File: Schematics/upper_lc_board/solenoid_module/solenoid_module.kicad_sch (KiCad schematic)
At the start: 21 parts

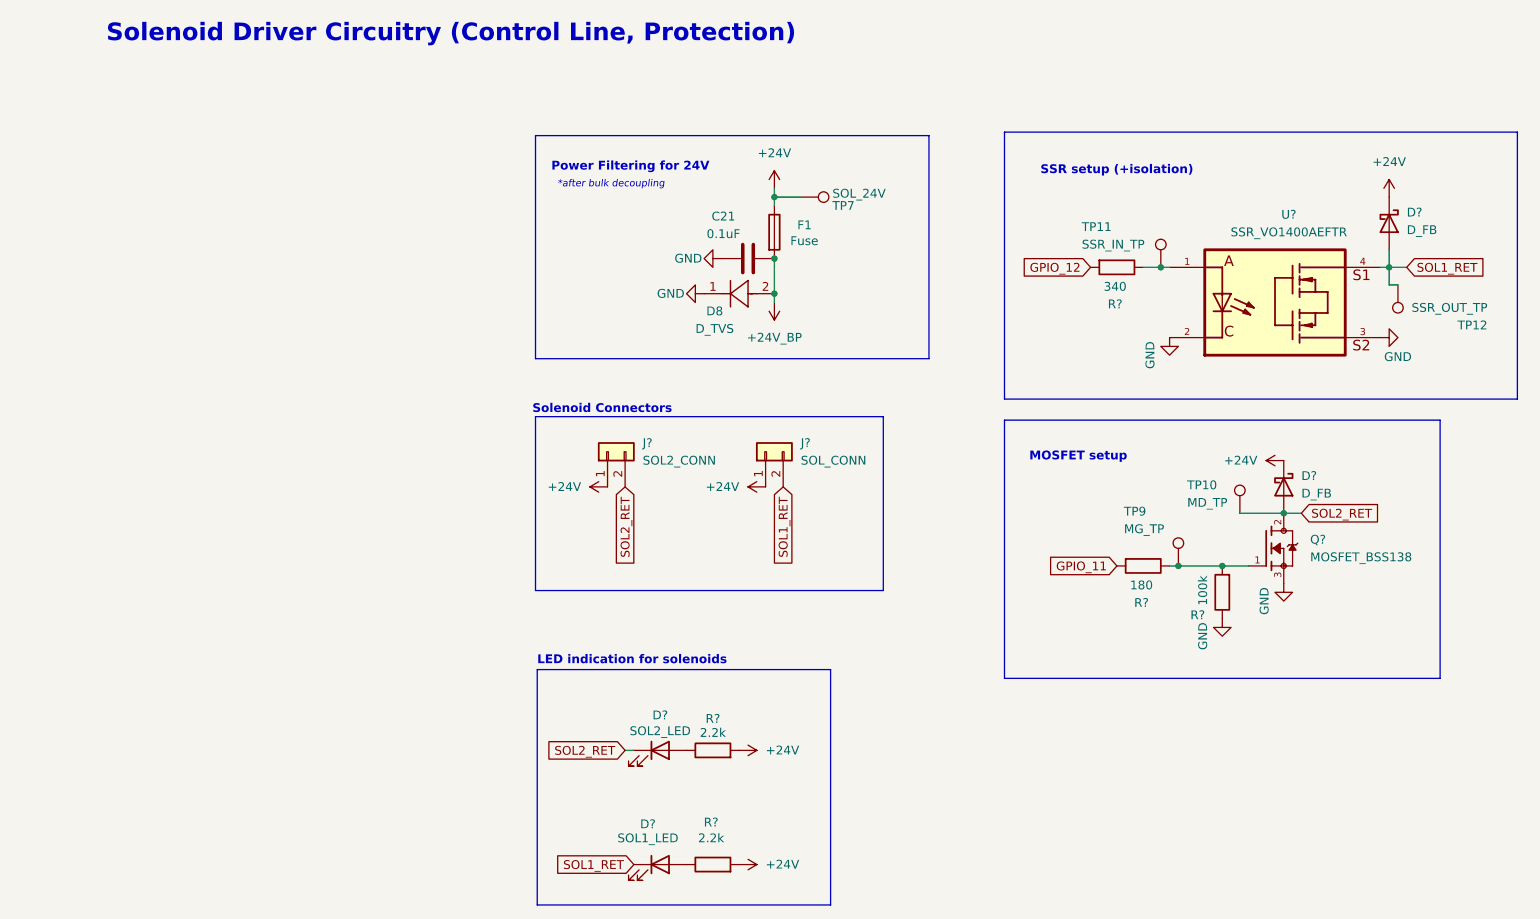
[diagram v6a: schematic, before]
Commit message: Updated all gpio for better routing, > - removed diode array, and 5v sensing > - added dedicated clk generator for adc
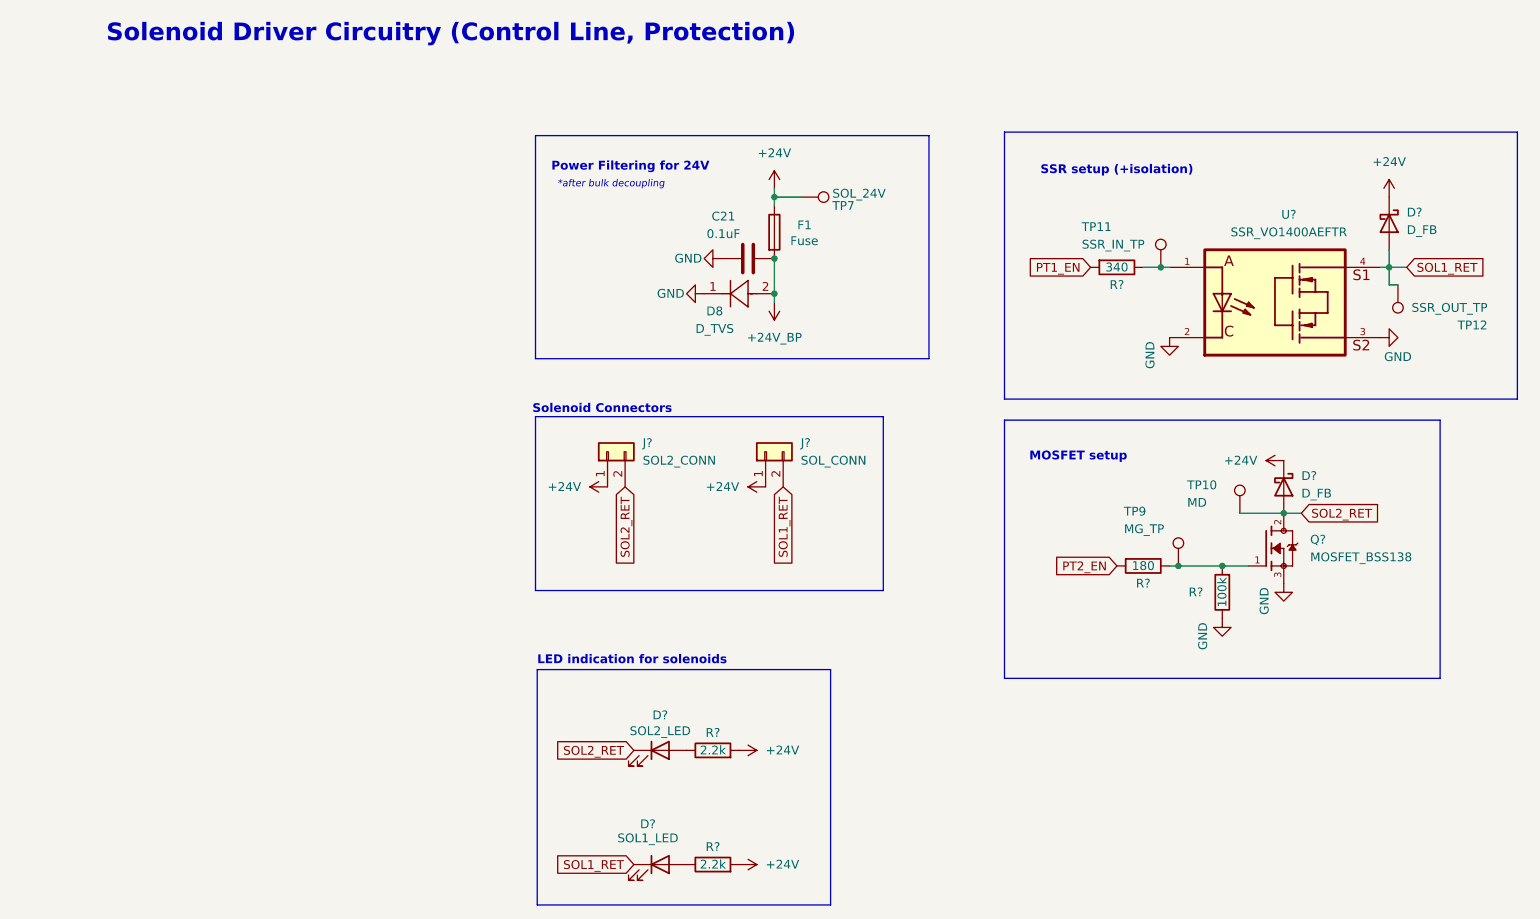
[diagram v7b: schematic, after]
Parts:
- TP10: value MD_TP -> MD
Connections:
- net GPIO_11 renamed PT2_EN
- net GPIO_12 renamed PT1_EN
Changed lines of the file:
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@@
-	(wire
-		(pts
-			(xy 90.17 125.73) (xy 91.44 125.73)
-		)
-		(stroke
-			(width 0)
-			(type default)
-		)
-	)
 	(wire
 		(pts
@@
 		)
 	)
-	(global_label "GPIO_11"
+	(global_label "PT1_EN"
 		(shape input)
-		(at 161.29 99.06 180)
+		(at 157.48 55.88 180)
 		(fields_autoplaced yes)
 		(effects
@@
 		)
 		(property "Intersheetrefs" "${INTERSHEET_REFS}"
-			(at 150.4429 99.06 0)
+			(at 147.6006 55.88 0)
 			(effects
 				(font
@@
 		)
 	)
+	(global_label "PT2_EN"
+		(shape input)
+		(at 161.29 99.06 180)
+		(fields_autoplaced yes)
+		(effects
+			(font
+				(size 1.27 1.27)
+			)
+			(justify right)
+		)
+		(property "Intersheetrefs" "${INTERSHEET_REFS}"
+			(at 151.4106 99.06 0)
+			(effects
+				(font
+					(size 1.27 1.27)
+				)
+				(justify right)
+				(hide yes)
+			)
+		)
+	)
 	(global_label "SOL1_RET"
 		(shape input)
@@
 		)
 	)
-	(global_label "GPIO_12"
-		(shape input)
-		(at 157.48 55.88 180)
-		(fields_autoplaced yes)
-		(effects
-			(font
-				(size 1.27 1.27)
-			)
-			(justify right)
-		)
-		(property "Intersheetrefs" "${INTERSHEET_REFS}"
-			(at 146.6329 55.88 0)
-			(effects
-				(font
-					(size 1.27 1.27)
-				)
-				(justify right)
-				(hide yes)
-			)
-		)
-	)
 	(global_label "SOL2_RET"
 		(shape input)
@@
 	(global_label "SOL2_RET"
 		(shape input)
-		(at 90.17 125.73 180)
+		(at 91.44 125.73 180)
 		(fields_autoplaced yes)
 		(effects
@@
 		)
 		(property "Intersheetrefs" "${INTERSHEET_REFS}"
-			(at 78.053 125.73 0)
+			(at 79.323 125.73 0)
 			(effects
 				(font
@@
 		(dnp no)
 		(property "Reference" "R?"
-			(at 161.036 61.214 90)
+			(at 161.29 58.42 90)
 			(effects
 				(font
@@
 		)
 		(property "Value" "340"
-			(at 161.036 58.674 90)
+			(at 161.29 55.88 90)
 			(effects
 				(font
@@
 			)
 		)
-		(property "Value" "MD_TP"
+		(property "Value" "MD"
 			(at 171.45 89.916 0)
 			(effects
@@
 		(dnp no)
 		(property "Reference" "R?"
-			(at 102.616 136.144 90)
+			(at 102.87 139.7 90)
 			(effects
 				(font
@@
 		)
 		(property "Value" "2.2k"
-			(at 102.616 138.43 90)
+			(at 102.87 142.24 90)
 			(effects
 				(font
@@
 		(dnp no)
 		(property "Reference" "R?"
-			(at 172.974 106.172 0)
+			(at 172.72 102.87 0)
 			(effects
 				(font
@@
 		)
 		(property "Value" "100k"
-			(at 173.736 102.616 90)
+			(at 176.53 102.87 90)
 			(effects
 				(font
@@
 		(dnp no)
 		(property "Reference" "R?"
-			(at 164.846 104.394 90)
+			(at 165.1 101.6 90)
 			(effects
 				(font
@@
 		)
 		(property "Value" "180"
-			(at 164.846 101.854 90)
+			(at 165.1 99.06 90)
 			(effects
 				(font
@@
 		(dnp no)
 		(property "Reference" "R?"
-			(at 102.87 121.158 90)
+			(at 102.87 123.19 90)
 			(effects
 				(font
@@
 		)
 		(property "Value" "2.2k"
-			(at 102.87 123.19 90)
-			(effects
-				(font
+			(at 102.87 125.73 90)
+			(effects
+				(font

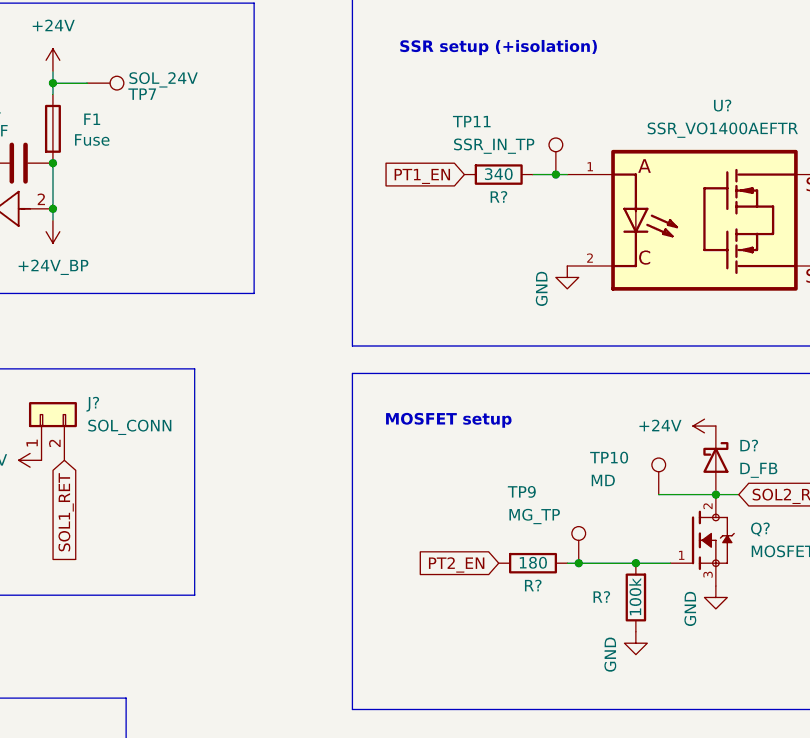
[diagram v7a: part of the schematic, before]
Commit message: fixed pin naming convention and updated gpios for better routing
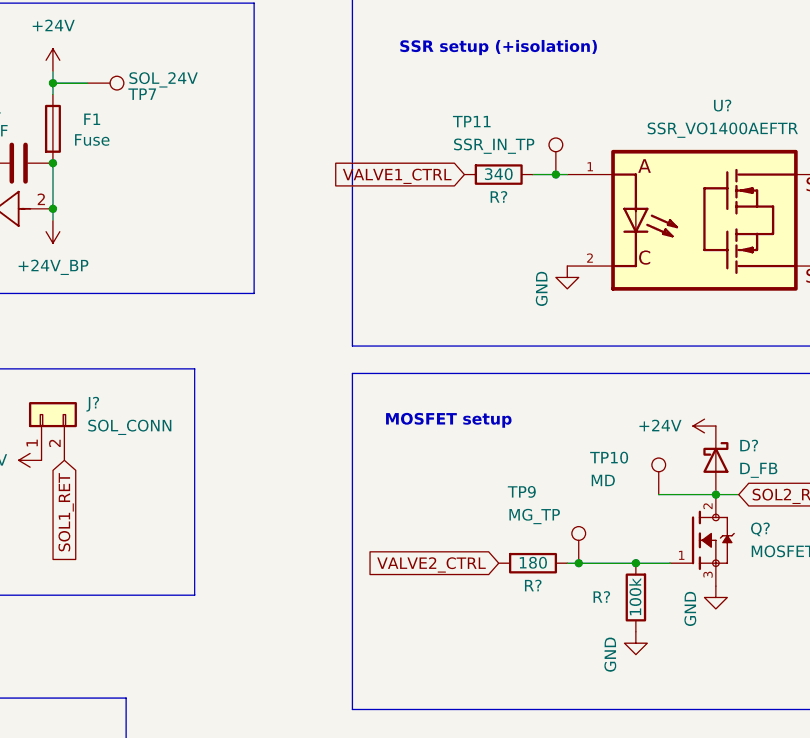
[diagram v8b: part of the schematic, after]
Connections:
- net PT1_EN renamed VALVE1_CTRL
- net PT2_EN renamed VALVE2_CTRL
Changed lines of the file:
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@@
 		)
 	)
-	(global_label "PT1_EN"
+	(global_label "VALVE1_CTRL"
 		(shape input)
 		(at 157.48 55.88 180)
@@
 		)
 		(property "Intersheetrefs" "${INTERSHEET_REFS}"
-			(at 147.6006 55.88 0)
+			(at 142.3391 55.88 0)
 			(effects
 				(font
@@
 		)
 	)
-	(global_label "PT2_EN"
+	(global_label "VALVE2_CTRL"
 		(shape input)
 		(at 161.29 99.06 180)
@@
 		)
 		(property "Intersheetrefs" "${INTERSHEET_REFS}"
-			(at 151.4106 99.06 0)
+			(at 146.1491 99.06 0)
 			(effects
 				(font
